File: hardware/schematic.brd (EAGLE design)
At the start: 50.8 x 38.1 mm, 28 parts, among them J1 SMA_EDGE, U1 HX1

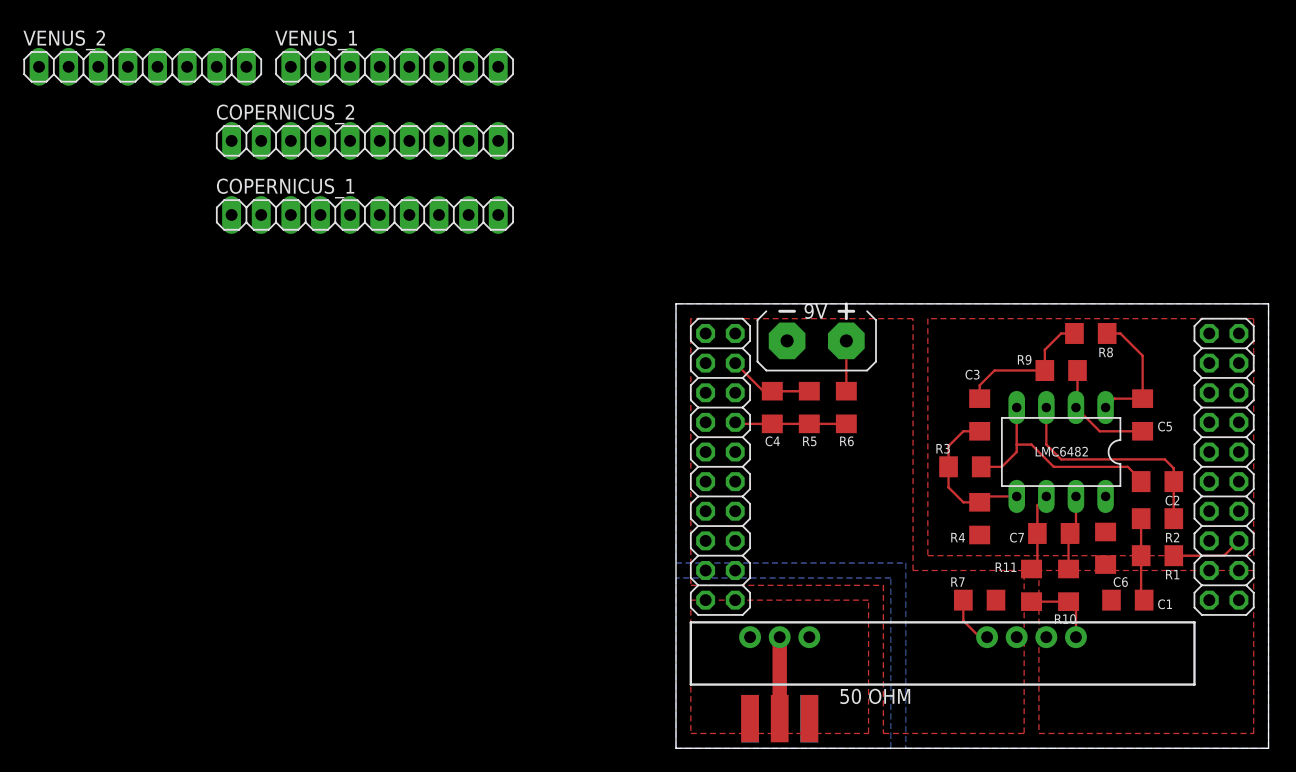
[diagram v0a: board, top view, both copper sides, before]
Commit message: Update PCB to include VRM module, change all components to 0805, and upgrade silkscreen
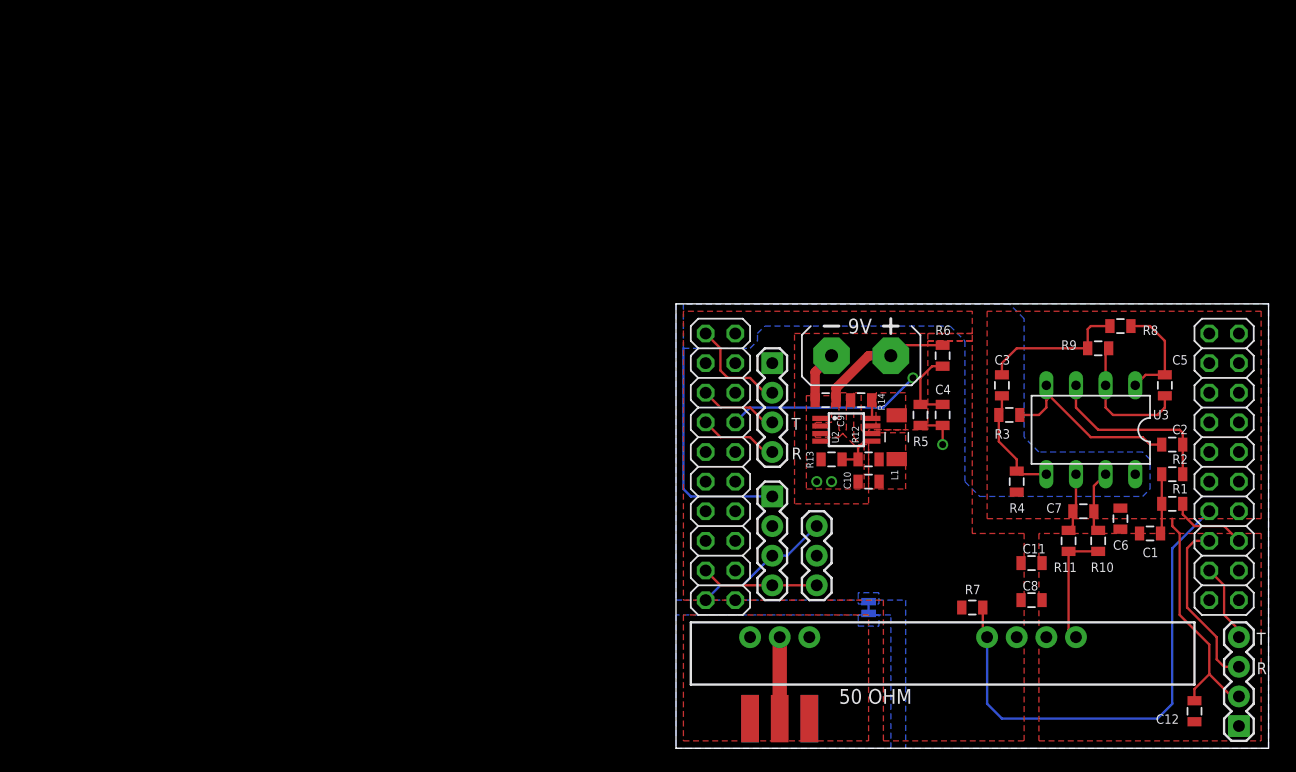
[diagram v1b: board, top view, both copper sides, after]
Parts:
- removed COPERNICUS_1, COPERNICUS_2: (no value), pinhead:1X10
- removed LMC6482: (no value), ic-package:DIL08
- removed VENUS_1, VENUS_2: (no value), pinhead:1X08
- added C10, C11, C9: 10u, SparkFun-Passives:0805
- added C12, C8: 0.1uF, SparkFun-Passives:0805
- added JP1: I2C IN, SparkFun-Connectors:1X03
- added JP2: SENSORS, SparkFun-Connectors:1X04
- added JP3: VENUS, SparkFun-Connectors:1X04
- added JP4: COPERNICUS, SparkFun-Connectors:1X04
- added L1: 2.2u, HAB:1008
- added R12: 430K, SparkFun-Passives:0805
- added R13: 82K, SparkFun-Passives:0805
- added R14: 100K, SparkFun-Passives:0805
- added SJ1: JUMPER-PAD-2-NC_BY_TRACE, SparkFun-Passives:PAD-JUMPER-2-NC_BY_TRACE_YES_SILK
- added U$1: (no value), HAB:GARAGE
- added U2: TPS62160, HAB:MSOP8
- added U3: LMC6482, ic-package:DIL08
- C1, C2, C3, C5, C6, C7, R1, R10, R11, R2, R3, R4, R5, R6, R7, R8, R9: device SparkFun-Passives:1206 -> SparkFun-Passives:0805
- C4: value (none) -> 0.1uF; device SparkFun-Passives:1206 -> SparkFun-Passives:0805
- moved C4 14.6 mm to (22.9, 28.6), turned to 270 degrees
- moved R5 9.55 mm to (21.0, 28.6), turned to 90 degrees
- moved R6 9.38 mm to (22.9, 33.7)
- moved C1 6.02 mm to (40.6, 18.4)
- moved R3 5.85 mm to (28.6, 28.6)
- moved R11 4.96 mm to (33.7, 17.8)
- moved R1 4.62 mm to (42.5, 21.0)
- moved R10 4.58 mm to (36.2, 17.8)
- moved R4 4.49 mm to (29.2, 22.9)
- moved R2 4.02 mm to (42.5, 23.5)
- moved G1 4.02 mm to (15.9, 33.7)
- moved R9 3.70 mm to (36.2, 34.3)
- moved C2 3.42 mm to (42.5, 26.0)
- moved C3 3.18 mm to (27.9, 31.1)
- moved C7 3.18 mm to (34.9, 20.3)
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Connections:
- new net CRX: JP4.4, TIVA_2.17
- new net CTX: JP4.3, TIVA_2.15
- new net FB5: R12.1, R13.2, U2.5
- new net PG5: R14.1, U2.8
- new net SCL: JP1.3, JP2.4, TIVA_1.17
- new net SDA: JP1.1, JP2.3, TIVA_1.19
- new net SW5: L1.1, U2.7
- new net VRX: JP3.4, TIVA_1.7
- new net VTX: JP3.3, TIVA_1.5
- net +3V3: now also C12.1, JP2.1, JP3.2, JP4.2, TIVA_1.1, U3.8; no longer LMC6482.8
- net +5V: now also C10.1, C11.1, C8.1, L1.2, R12.2, R14.2, U2.6
- net +9V: now also C9.1, U2.2, U2.3
- net EN: now also TIVA_2.13
- net GNDA: now also C10.2, C11.2, C12.2, C8.2, C9.2, JP1.2, JP2.2, JP3.1, JP4.1, R13.1, SJ1.1, U2.1, U2.4, U3.4; no longer LMC6482.4
- net HPFB: now also U3.6; no longer LMC6482.6
- net HPOUT: now also U3.5; no longer LMC6482.5
- net LPFB: now also U3.2; no longer LMC6482.2
- net LPOUT: now also U3.1; no longer LMC6482.1
- net PWMF2: now also U3.3; no longer LMC6482.3
- net RFGND: now also SJ1.2
- net TXF: now also U3.7; no longer LMC6482.7
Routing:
- net +3V3: track 0.00 -> 49.7 mm
- net EN: track 4.39 -> 43.2 mm
- net CTX: track 0.00 -> 14.9 mm
- net VBAT: track 9.58 -> 24.0 mm, vias 0 -> 1
- net SDA: track 0.00 -> 12.2 mm
- net SCL: track 0.00 -> 10.1 mm
- net +9V: track 4.31 -> 11.7 mm
- net VRX: track 0.00 -> 6.77 mm
- net VTX: track 0.00 -> 6.77 mm
- net CRX: track 0.00 -> 6.77 mm
- net FB5: track 0.00 -> 3.81 mm
- net PWMF2: track 19.3 -> 15.5 mm
- net TXD: track 6.48 -> 10.2 mm
- net HPOUT: track 13.3 -> 9.85 mm
- net GNDA: track 26.8 -> 23.9 mm, vias 0 -> 3
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- added copper zone on layer 16, net +3V3
- added copper zone on layer 1, net +9V
- added copper zone on layer 1, net SW5
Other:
- board text added: "HAB Project, Revision B"
- board text added: "R"
- board text added: "RF GROUND"
- board text added: "T"
- board text added: "~stcarlso"

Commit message: Add another cool logo for testing purposes
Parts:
- added U$2: (no value), HAB:SWIFT
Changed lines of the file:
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@@
 <wire x1="0" y1="38.1" x2="0" y2="0" width="0" layer="20"/>
 <text x="13.97" y="3.81" size="1.27" layer="21">50 OHM</text>
-<text x="19.685" y="17.145" size="0.8128" layer="22" rot="MR0">RF GROUND</text>
+<text x="24.765" y="11.43" size="0.8128" layer="22" rot="MR0">RF GROUND</text>
 <wire x1="11.049" y1="22.098" x2="19.939" y2="22.098" width="0.1016" layer="51"/>
 <wire x1="19.939" y1="22.098" x2="19.939" y2="30.607" width="0.1016" layer="51"/>
@@
 <attribute name="VALUE" x="45.466" y="3.302" size="0.4064" layer="27" rot="R180"/>
 </element>
+<element name="U$2" library="HAB" package="SWIFT" value="" x="21.59" y="21.59" rot="MR0"/>
 </elements>
 <signals>

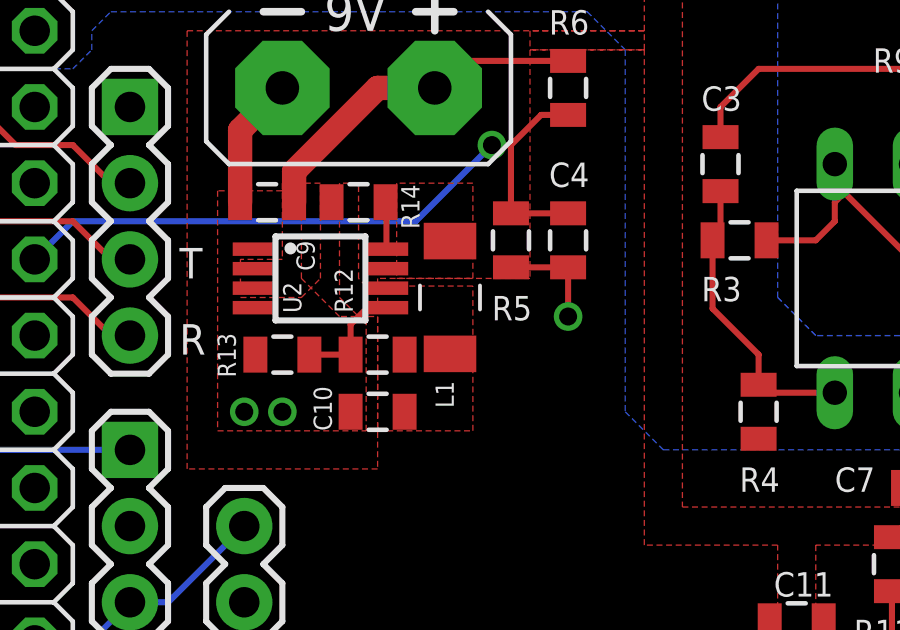
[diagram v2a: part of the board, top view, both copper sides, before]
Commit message: Fix pad to pad spacing on the "1008" inductor (not really) on the PCB. Existing board works, but is vulnerable to tombstoning if reflowed
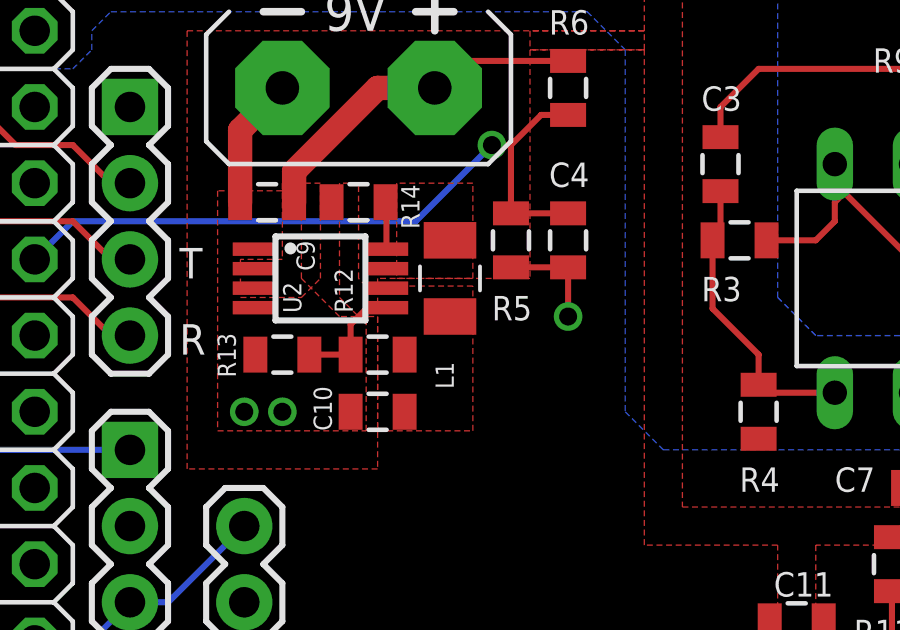
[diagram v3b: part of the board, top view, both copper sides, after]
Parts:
- moved L1 0.63 mm to (18.9, 27.3)
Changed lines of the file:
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@@
 <?xml version="1.0" encoding="utf-8"?>
 <!DOCTYPE eagle SYSTEM "eagle.dtd">
-<eagle version="7.3.0">
+<eagle version="7.4.0">
 <drawing>
 <settings>
@@
 <attribute name="NAME" x="13.97" y="26.155" size="0.6096" layer="25" rot="R90"/>
 </element>
-<element name="L1" library="HAB" package="1008" value="2.2u" x="18.923" y="26.67" smashed="yes">
-<attribute name="NAME" x="19.05" y="22.987" size="0.6096" layer="25" rot="R90"/>
-<attribute name="VALUE" x="18.8468" y="26.305" size="0.3048" layer="27" rot="R90"/>
+<element name="L1" library="HAB" package="1008" value="2.2u" x="18.923" y="27.305" smashed="yes">
+<attribute name="NAME" x="19.05" y="23.622" size="0.6096" layer="25" rot="R90"/>
+<attribute name="VALUE" x="18.8468" y="26.94" size="0.3048" layer="27" rot="R90"/>
 </element>
 <element name="R12" library="SparkFun-Passives" package="0805" value="430K" x="16.51" y="24.765" smashed="yes">
